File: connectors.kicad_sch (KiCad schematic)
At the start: 4 parts, among them CN10 Conn_02x17_Odd_Even, CN7 Conn_02x10_Odd_Even, CN8 Conn_02x08_Odd_Even, CN9 Conn_02x15_Odd_Even

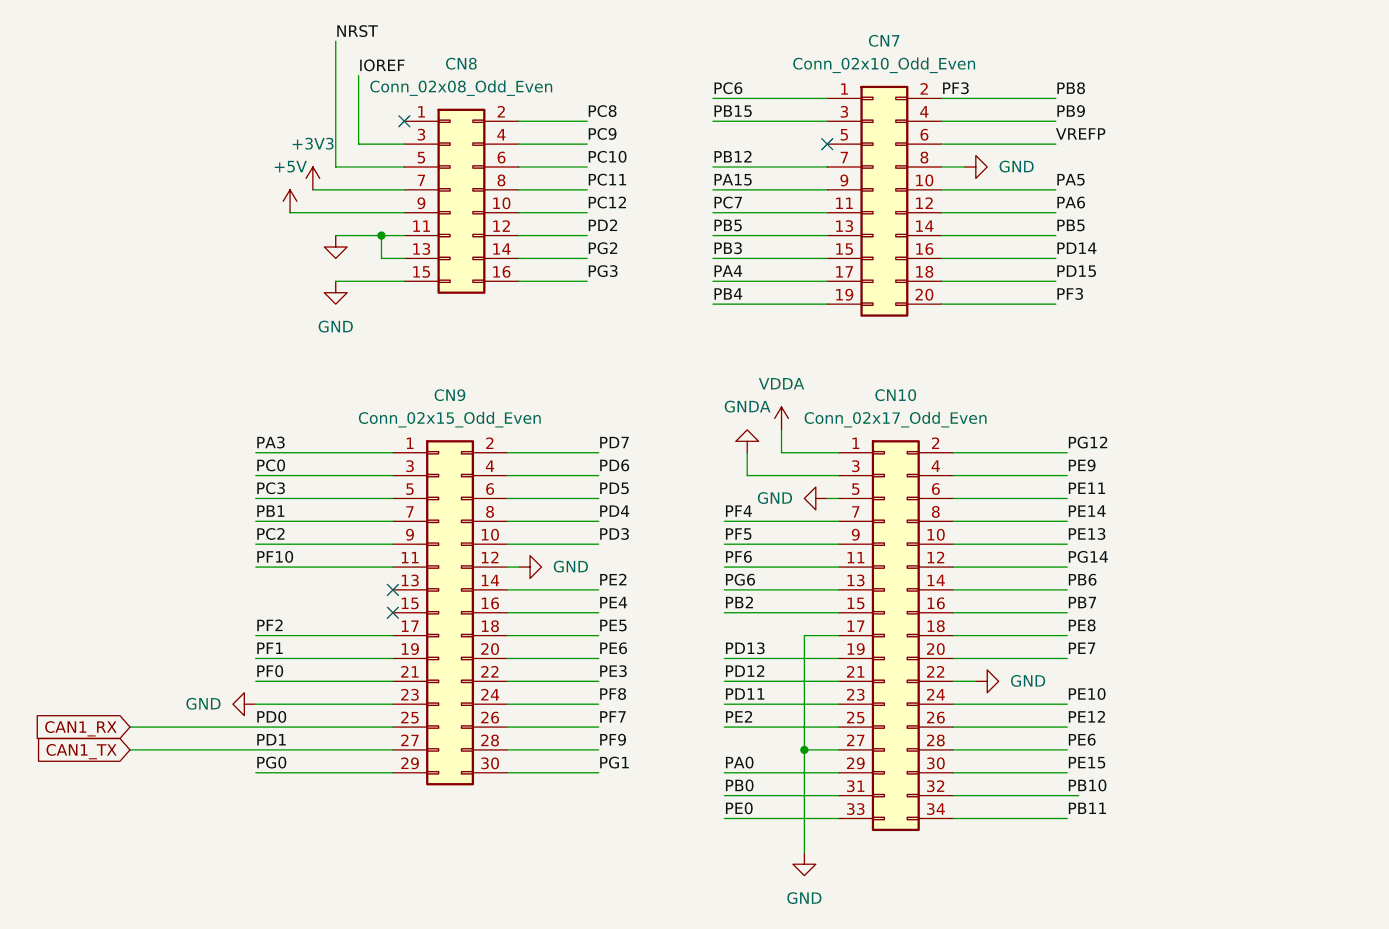
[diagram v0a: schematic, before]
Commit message: connect CANs to ZIO
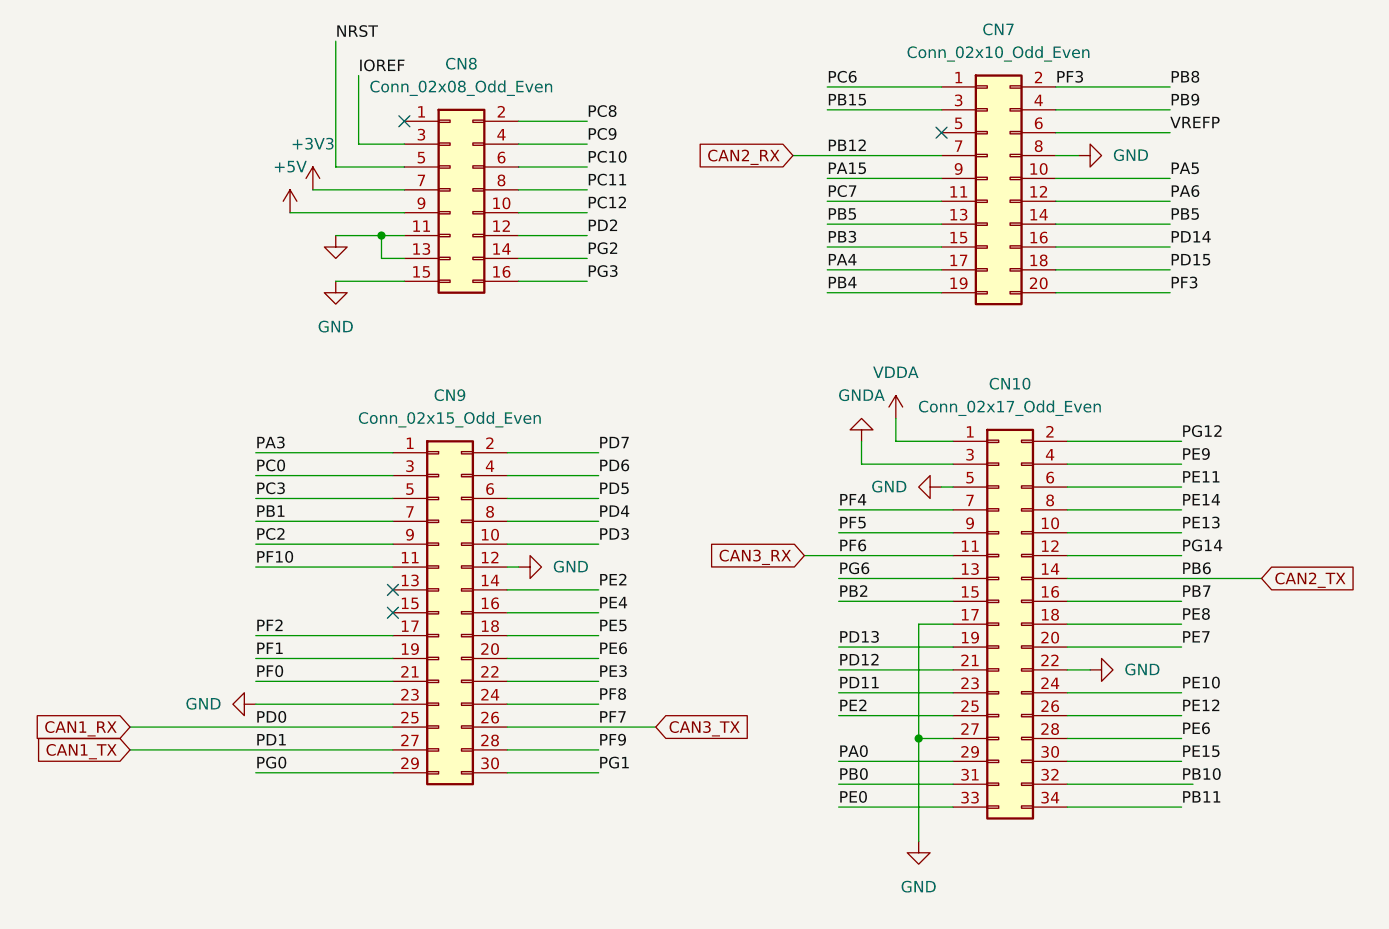
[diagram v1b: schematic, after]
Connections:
- net PB12 renamed CAN2_RX
- net PB6 renamed CAN2_TX
- net PF6 renamed CAN3_RX
- net PF7 renamed CAN3_TX
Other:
- moved on the sheet: CN10, CN7
